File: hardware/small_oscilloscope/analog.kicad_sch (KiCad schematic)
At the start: 41 parts, among them J1 Conn_Coaxial, J3 Conn_Coaxial, Q1 NTR5103NT1G, Q2 NTR5103NT1G, Q3 NTR5103NT1G, Q4 NTR5103NT1G, Q5 NTR5103NT1G, Q6 NTR5103NT1G, Q7 NTR5103NT1G, Q8 NTR5103NT1G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

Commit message: 250627 circuit
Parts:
- C1: renamed from C2; footprint (none) -> Capacitor_SMD:C_0402_1005Metric_Pad0.74x0.62mm_HandSolder
- C2: renamed from C1; footprint (none) -> Capacitor_SMD:C_0402_1005Metric_Pad0.74x0.62mm_HandSolder
- Q1: renamed from Q5; footprint (none) -> Package_TO_SOT_SMD:SOT-23_Handsoldering
- Q2: renamed from Q1; footprint (none) -> Package_TO_SOT_SMD:SOT-23_Handsoldering
- Q3: renamed from Q6; footprint (none) -> Package_TO_SOT_SMD:SOT-23_Handsoldering
- Q4: renamed from Q2; footprint (none) -> Package_TO_SOT_SMD:SOT-23_Handsoldering
- Q5: renamed from Q7; footprint (none) -> Package_TO_SOT_SMD:SOT-23_Handsoldering
- Q6: renamed from Q3; footprint (none) -> Package_TO_SOT_SMD:SOT-23_Handsoldering
- Q7: renamed from Q8; footprint (none) -> Package_TO_SOT_SMD:SOT-23_Handsoldering
- Q8: renamed from Q4; footprint (none) -> Package_TO_SOT_SMD:SOT-23_Handsoldering
- R10: renamed from R14; value 1k -> 1K; footprint (none) -> Resistor_THT:R_Axial_DIN0207_L6.3mm_D2.5mm_P10.16mm_Horizontal
- R11: renamed from R15; value 1k -> 1K; footprint (none) -> Resistor_THT:R_Axial_DIN0207_L6.3mm_D2.5mm_P10.16mm_Horizontal
- R12: renamed from R5; value 1k -> 1K; footprint (none) -> Resistor_THT:R_Axial_DIN0207_L6.3mm_D2.5mm_P10.16mm_Horizontal
- R13: renamed from R6; value 1k -> 1K; footprint (none) -> Resistor_THT:R_Axial_DIN0207_L6.3mm_D2.5mm_P10.16mm_Horizontal
- R14: renamed from R16; footprint (none) -> Resistor_THT:R_Axial_DIN0207_L6.3mm_D2.5mm_P10.16mm_Horizontal
- R15, R19: renamed from R7; footprint (none) -> Resistor_THT:R_Axial_DIN0207_L6.3mm_D2.5mm_P10.16mm_Horizontal
- R16: renamed from R17; footprint (none) -> Resistor_THT:R_Axial_DIN0207_L6.3mm_D2.5mm_P10.16mm_Horizontal
- R17: renamed from R8; footprint (none) -> Resistor_THT:R_Axial_DIN0207_L6.3mm_D2.5mm_P10.16mm_Horizontal
- R18: footprint (none) -> Resistor_THT:R_Axial_DIN0207_L6.3mm_D2.5mm_P10.16mm_Horizontal
- R2: renamed from R10; footprint (none) -> Resistor_THT:R_Axial_DIN0207_L6.3mm_D2.5mm_P10.16mm_Horizontal
- R20: renamed from R19; value 1k -> 1K; footprint (none) -> Resistor_THT:R_Axial_DIN0207_L6.3mm_D2.5mm_P10.16mm_Horizontal
- R21: renamed from R20; value 3k -> 3K; footprint (none) -> Resistor_THT:R_Axial_DIN0207_L6.3mm_D2.5mm_P10.16mm_Horizontal
- R22: renamed from R8; value 1k -> 1K; footprint (none) -> Resistor_THT:R_Axial_DIN0207_L6.3mm_D2.5mm_P10.16mm_Horizontal
- R23: renamed from R9; value 3k -> 3K; footprint (none) -> Resistor_THT:R_Axial_DIN0207_L6.3mm_D2.5mm_P10.16mm_Horizontal
- R3: renamed from R11; value 10k -> 10K; footprint (none) -> Resistor_THT:R_Axial_DIN0207_L6.3mm_D2.5mm_P10.16mm_Horizontal
- R4: renamed from R1; footprint (none) -> Resistor_THT:R_Axial_DIN0207_L6.3mm_D2.5mm_P10.16mm_Horizontal
- R5: renamed from R2; value 10k -> 10K; footprint (none) -> Resistor_THT:R_Axial_DIN0207_L6.3mm_D2.5mm_P10.16mm_Horizontal
- R6: renamed from R12; value 100k -> 100K; footprint (none) -> Resistor_THT:R_Axial_DIN0207_L6.3mm_D2.5mm_P10.16mm_Horizontal
- R7: renamed from R13; value 11k -> 11K; footprint (none) -> Resistor_THT:R_Axial_DIN0207_L6.3mm_D2.5mm_P10.16mm_Horizontal
- R8: renamed from R3; value 100k -> 100K; footprint (none) -> Resistor_THT:R_Axial_DIN0207_L6.3mm_D2.5mm_P10.16mm_Horizontal
- R9: renamed from R4; value 11k -> 11K; footprint (none) -> Resistor_THT:R_Axial_DIN0207_L6.3mm_D2.5mm_P10.16mm_Horizontal
- U6: renamed from U5; footprint (none) -> Package_SO:SOIC-14_3.9x8.7mm_P1.27mm
- U7: renamed from U6; footprint (none) -> Package_DIP:DIP-8_W7.62mm_LongPads
- U8: renamed from U9; footprint (none) -> Package_DIP:DIP-8_W7.62mm_LongPads
- renumbered J1 to J4, U7 to U2, U8 to U3, U1 to U4, U3 to U5
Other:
- note added: "Q 1,2 | 7, 8 : DC/AC Enable Q 3,4 | 9,10 : attu 1 [0,0]:100% , [1,0]:10% , [0,1]:1% Q 5,6 | 11,12 : attu 2 [0,0]:100% , [0,1]:50% , [1,0]:20% Vo = 8v + 2.5 [V]"

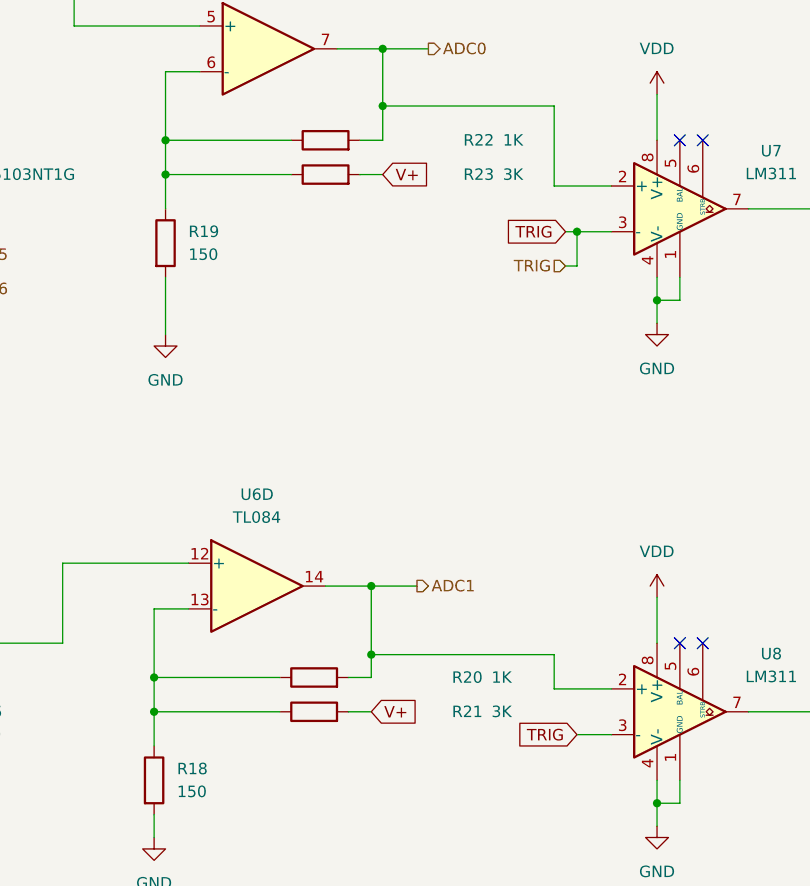
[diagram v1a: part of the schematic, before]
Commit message: feat: 오실로스코프 회로 설계 업데이트
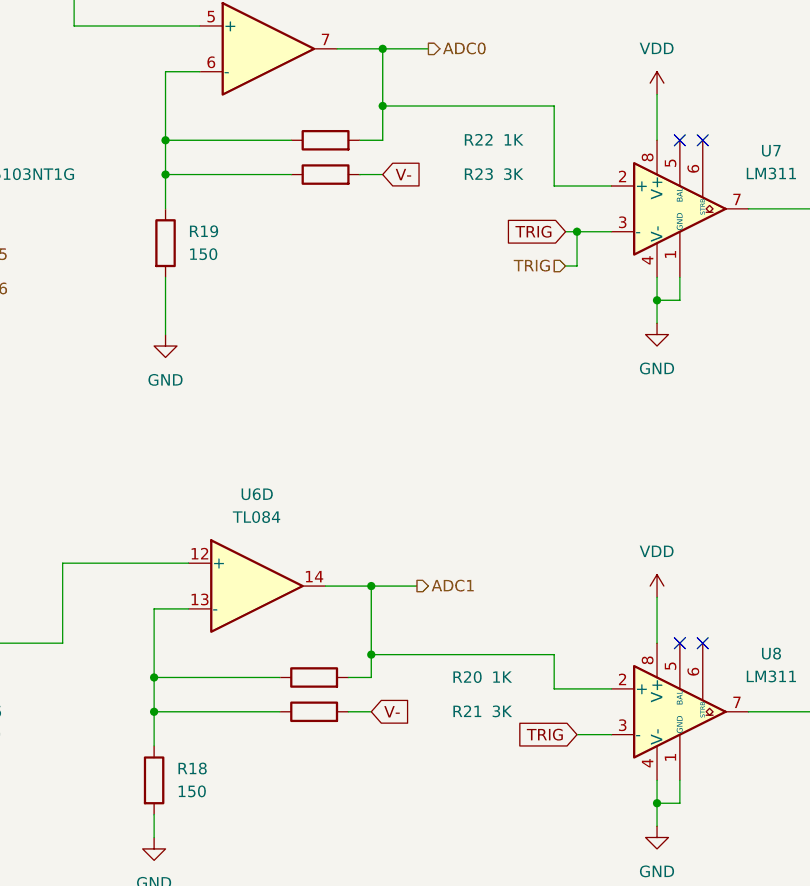
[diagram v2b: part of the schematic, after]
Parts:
- U2, U3, U4, U5: footprint Package_TO_SOT_SMD:SOT-23-5_HandSoldering -> Package_TO_SOT_SMD:SOT-23-5
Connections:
- net V+: no longer R21.2, R23.2
- net V-: now also R21.2, R23.2
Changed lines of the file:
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@@
 		)
 	)
-	(global_label "V+"
+	(global_label "V-"
 		(shape input)
 		(at 215.9 139.7 0)
@@
 		)
 	)
-	(global_label "V+"
+	(global_label "V-"
 		(shape input)
 		(at 217.17 80.01 0)
@@
 			)
 		)
-		(property "Footprint" "Package_TO_SOT_SMD:SOT-23-5_HandSoldering"
+		(property "Footprint" "Package_TO_SOT_SMD:SOT-23-5"
 			(at 58.42 68.58 0)
 			(effects
@@
 			)
 		)
-		(property "Footprint" "Package_TO_SOT_SMD:SOT-23-5_HandSoldering"
+		(property "Footprint" "Package_TO_SOT_SMD:SOT-23-5"
 			(at 58.42 46.99 0)
 			(effects
@@
 			)
 		)
-		(property "Footprint" "Package_TO_SOT_SMD:SOT-23-5_HandSoldering"
+		(property "Footprint" "Package_TO_SOT_SMD:SOT-23-5"
 			(at 57.15 132.08 0)
 			(effects
@@
 			)
 		)
-		(property "Footprint" "Package_TO_SOT_SMD:SOT-23-5_HandSoldering"
+		(property "Footprint" "Package_TO_SOT_SMD:SOT-23-5"
 			(at 57.15 153.67 0)
 			(effects

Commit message: oscilliscope first success
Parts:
- removed Q2, Q3: NTR5103NT1G, Package_TO_SOT_SMD:SOT-23_Handsoldering, symbol Transistor_FET:Q_NMOS_GSD
- removed R21: 3K, Resistor_THT:R_Axial_DIN0207_L6.3mm_D2.5mm_P10.16mm_Horizontal, symbol Device:R
- removed U2, U3, U4, U5: TMUX1101DBV, Package_TO_SOT_SMD:SOT-23-5, symbol Analog_Switch:TMUX1101DBV
- added K1, K2, K3, K4: FINDER-40.41, Relay_THT:Relay_SPDT_Finder_40.41, symbol Relay:FINDER-40.41
- added Q12, Q3, Q7, Q8: 2SC4671, Package_TO_SOT_SMD:SOT-523, symbol Transistor_BJT:2SC4213
- added R33, R38, R51, R52: 3k, Resistor_SMD:R_0402_1005Metric_Pad0.72x0.64mm_HandSolder, symbol Device:R
- added R35, R42, R43: 3K6, Resistor_THT:R_Axial_DIN0207_L6.3mm_D2.5mm_P10.16mm_Horizontal, symbol Device:R
- C3: renamed from C2; now left out of the parts list
- C4: renamed from C1; now left out of the parts list
- Q10: renamed from Q5; value NTR5103NT1G -> BSS138; now left out of the parts list
- Q11: renamed from Q7; value NTR5103NT1G -> BSS138; now left out of the parts list
- Q4: value NTR5103NT1G -> BSS138; now left out of the parts list
- Q5: renamed from Q6; value NTR5103NT1G -> BSS138; now left out of the parts list
- Q6: renamed from Q8; value NTR5103NT1G -> BSS138; now left out of the parts list
- Q9: renamed from Q1; value NTR5103NT1G -> BSS138; now left out of the parts list
- R25: renamed from R4; now left out of the parts list
- R26: renamed from R12; now left out of the parts list
- R28: renamed from R8; now left out of the parts list
- R29: renamed from R13; now left out of the parts list
- R30: renamed from R15; value 500 -> 500R; now left out of the parts list
- R31: renamed from R17; value 500 -> 500R; now left out of the parts list
- R32: renamed from R9; now left out of the parts list
- R34: renamed from R22; now left out of the parts list
- R36: renamed from R23; value 3K -> 3K6; now left out of the parts list
- R37: renamed from R19; value 150 -> 150R; now left out of the parts list
- R39: renamed from R2; now left out of the parts list
- R40: renamed from R10; now left out of the parts list
- R41: renamed from R20; now left out of the parts list
- R45: renamed from R6; now left out of the parts list
- R46: renamed from R11; now left out of the parts list
- R47: renamed from R14; value 500 -> 500R; now left out of the parts list
- R48: renamed from R16; value 500 -> 500R; now left out of the parts list
- R49: renamed from R18; value 150 -> 150R; now left out of the parts list
- R50: renamed from R7; now left out of the parts list
- U3: renamed from U6; now left out of the parts list
- renumbered J4 to J2, R5 to R27, R3 to R44, U7 to U4, U8 to U5
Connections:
- net GND: now also R32.2, R50.2, Q12.2 (E), Q3.2 (E), Q7.2 (E), Q8.2 (E)
- net Q1: now also R33.1
- net Q3: now also R38.2; no longer Q4.1 (G)
- net Q4: now also Q4.1 (G)
- net Q7: now also R51.1
- net Q9: now also R52.2
- net V-: now also R43.2
- net at R25.1: now also K1.11
- net at C3.1, J2.1 (In): now also K1.12
- net at R34.1, R37.1, U3.6 (-): now also R35.1; no longer R36.1
- net at R25.2, R27.1, U3.3 (+): now also K2.11; no longer R28.1
- net at R39.2, R44.1, U3.10 (+): now also K4.11; no longer R45.1
- net at C3.2: now also K1.14
- net at C4.1, J3.1 (In): now also K3.12
- net at R27.2: now also Q4.3 (D)
- net at R41.1, R49.1, U3.13 (-): now also R42.1
- net at C4.2: now also K3.14
- net at R39.1: now also K3.11
- new net: Q3.1 (B), R33.2
- new net: R35.2, R36.1
- new net: Q12.1 (B), R52.1
- new net: K2.14, R28.1
- new net: R42.2, R43.1
- new net: K4.14, R45.1
- new net: K4.A1, Q12.3 (C)
- new net: K1.A1, Q3.3 (C)
- new net: Q8.1 (B), R51.2
- new net: K3.A1, Q8.3 (C)
- new net: Q7.1 (B), R38.1
- new net: K2.A1, Q7.3 (C)
- new net +5V: K1.A2, K2.A2, K3.A2, K4.A2
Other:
- note added: "5/3 = 12/(3*12/5) = 12/(7.2)"
- note added: "Q 1,2 | 7, 8 : DC/AC Enable Q 3,4 | 9,10 : attu 1 [0,0]:100% , [1,0]:10% , [0,1]:1% Q 5,6 | 11,12 : attu 2 [0,0]:100% , [0,1]:50% , [1,0]:20% Vo = 8v + 3.3/2 [V]"
- note removed: "Q 1,2 | 7, 8 : DC/AC Enable Q 3,4 | 9,10 : attu 1 [0,0]:100% , [1,0]:10% , [0,1]:1% Q 5,6 | 11,12 : attu 2 [0,0]:100% , [0,1]:50% , [1,0]:20% Vo = 8v + 2.5 [V]"
- moved on the sheet: R28, R32, R45, R50

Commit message: fix: program tidy
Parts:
- added Q16: 2SA1015, Package_TO_SOT_THT:TO-92_Inline, symbol Transistor_BJT:2SA1015
- added Q17, Q18: Q_NPN_EBC, Package_TO_SOT_SMD:SOT-323_SC-70, symbol Transistor_BJT:Q_NPN_EBC
- added R88, R96: 100k, symbol Device:R
- added R97: 10k, symbol Device:R
- added R98: 1k, symbol Device:R
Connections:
- net +5V: now also Q16.1 (E), R88.1, R96.1; no longer K1.A2, K2.A2, K3.A2, K4.A2
- net GND: now also Q17.1 (E), Q18.1 (E)
- new net: Q18.3 (C), R96.2, R98.2
- new net: Q17.3 (C), R88.2, R97.2
- new net: Q18.2 (B), R97.1
- new net: Q16.3 (B), R98.1
- new net Qvsec: Q17.2 (B)
- new net Vsw: K1.A2, K2.A2, K3.A2, K4.A2, Q16.2 (C)
